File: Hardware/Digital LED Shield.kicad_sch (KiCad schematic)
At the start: 21 parts, among them IC2 LM66200DRLR, IC3 TPS259570DSGR, J1 Conn_02x10_Odd_Even, J2 Conn_01x03_Male, J3 Barrel_Jack_MountingPin, J4 Conn_01x02_Female, J5 Conn_01x03_Male, U1 SN74LVC1T45DBV

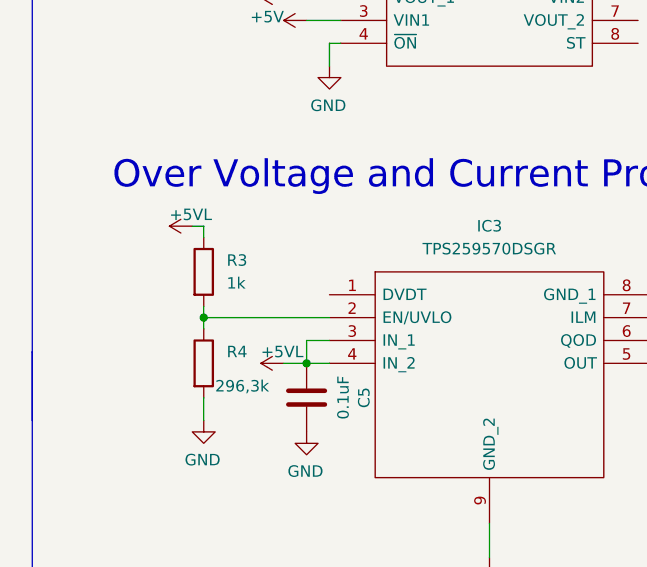
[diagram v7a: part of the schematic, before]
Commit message: update Overvoltage protection resistor value
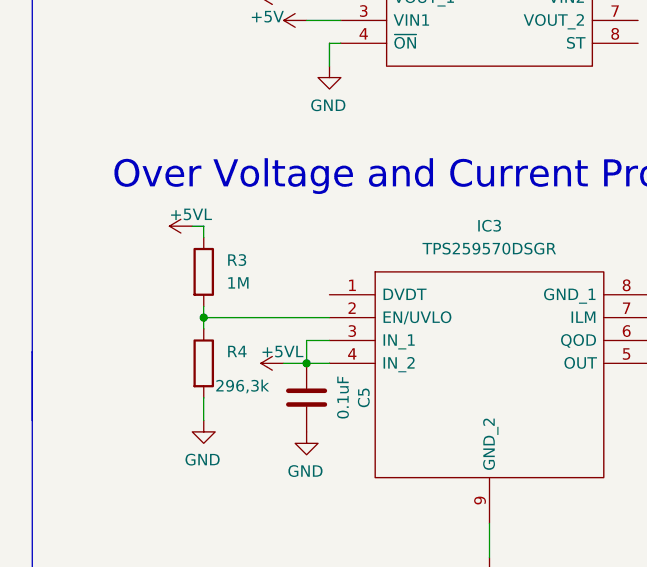
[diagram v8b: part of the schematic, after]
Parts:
- R3: value 1k -> 1M
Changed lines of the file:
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@@
       (effects (font (size 1.27 1.27)) (justify left))
     )
-    (property "Value" "1k" (id 1) (at 54.61 149.8599 0)
+    (property "Value" "1M" (id 1) (at 54.61 149.8599 0)
       (effects (font (size 1.27 1.27)) (justify left))
     )
@@
     )
     (path "/d9bfa772-72ce-4019-97ee-c7520e355f27"
-      (reference "R3") (unit 1) (value "1k") (footprint "Resistor_SMD:R_0603_1608Metric")
+      (reference "R3") (unit 1) (value "1M") (footprint "Resistor_SMD:R_0603_1608Metric")
     )
     (path "/ed44c660-2789-4a65-ad23-d189fa546730"
